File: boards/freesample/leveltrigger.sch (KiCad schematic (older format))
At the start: 23 parts, among them U10 PI6C59S6005, U9 HMC675LP3E

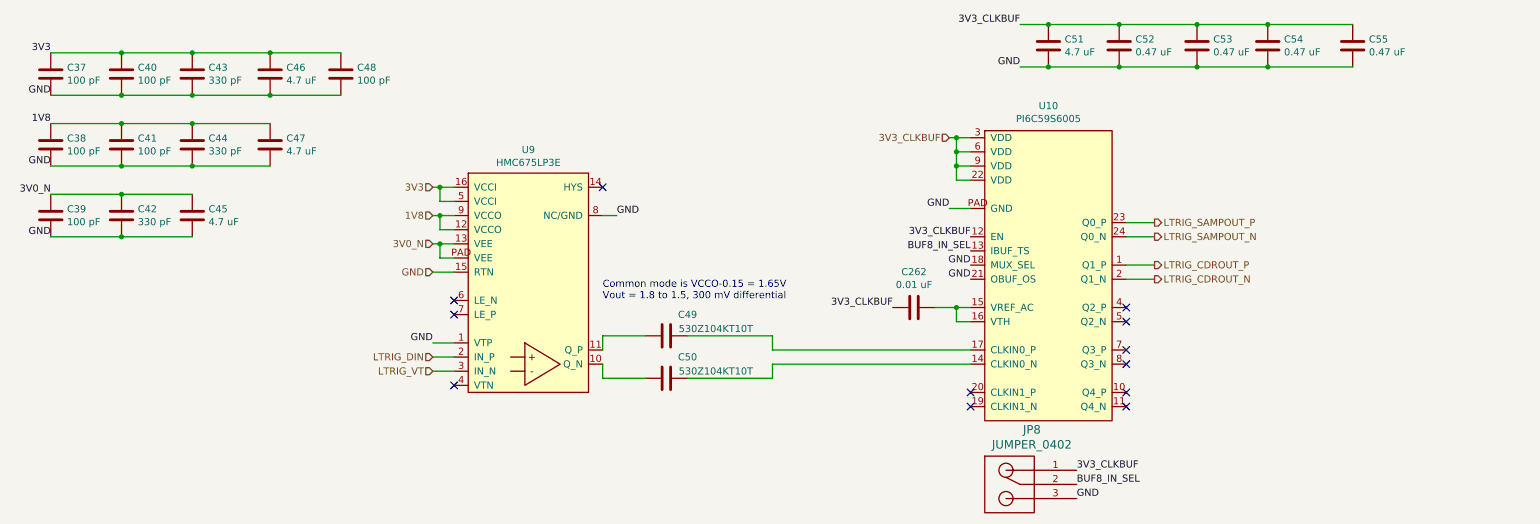
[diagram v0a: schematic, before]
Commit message: Added more test points. Started picking packages for passives. Continued schematic review.
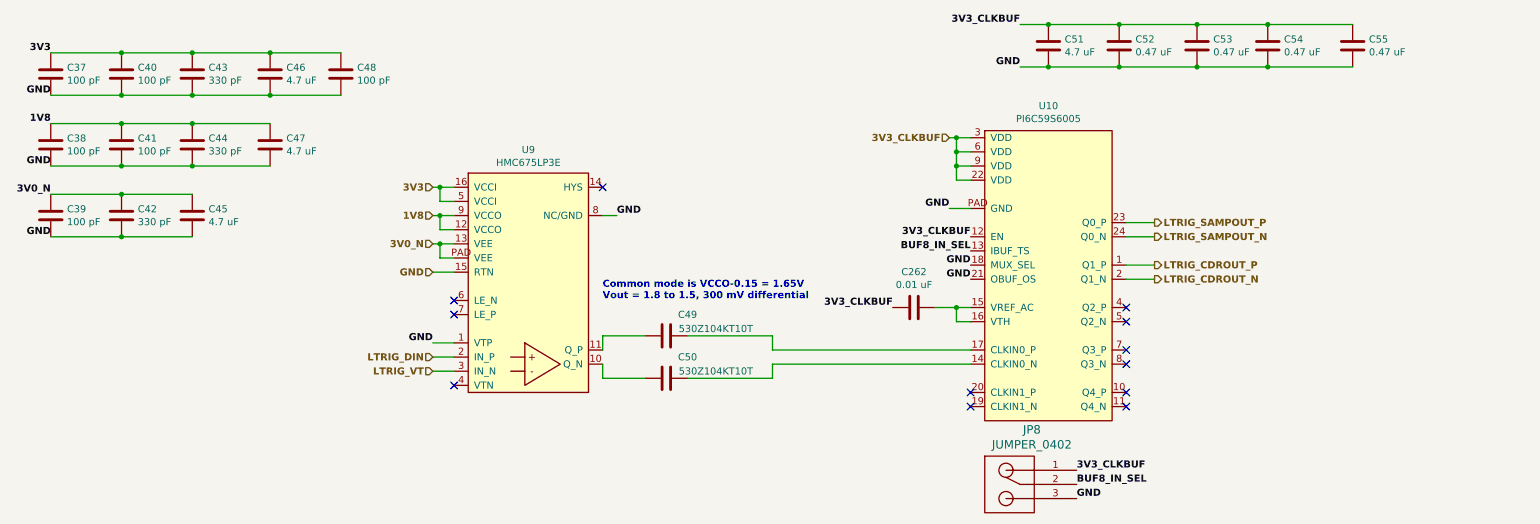
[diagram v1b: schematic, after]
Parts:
- C262, C52, C53, C54, C55: footprint (none) -> azonenberg_pcb:EIA_0402_CAP_NOSILK
- C37, C38, C39, C40, C41, C42, C43, C44, C48, C49, C50: footprint (none) -> azonenberg_pcb:EIA_0201_CAP_NOSILK
- C45, C46, C47, C51: footprint (none) -> azonenberg_pcb:EIA_0603_CAP_NOSILK
- JP8: footprint (none) -> azonenberg_pcb:EIA_0402_JUMPER
- U10: footprint (none) -> azonenberg_pcb:QFN_24_0.5MM_4x4MM
- U9: footprint (none) -> azonenberg_pcb:QFN_16_0.5MM_3x3MM
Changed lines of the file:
@@
 Comment4 ""
 $EndDescr
-Text HLabel 3750 3000 0    50   Input ~ 0
+Text HLabel 3750 3000 0    50   Input ~ 6
 LTRIG_DIN
-Text HLabel 8850 2350 2    50   Output ~ 0
+Text HLabel 8850 2350 2    50   Output ~ 6
 LTRIG_CDROUT_P
-Text HLabel 8850 2450 2    50   Output ~ 0
+Text HLabel 8850 2450 2    50   Output ~ 6
 LTRIG_CDROUT_N
-Text HLabel 3750 1800 0    50   Input ~ 0
+Text HLabel 3750 1800 0    50   Input ~ 6
 3V3
-Text HLabel 3750 2200 0    50   Input ~ 0
+Text HLabel 3750 2200 0    50   Input ~ 6
 3V0_N
-Text HLabel 3750 2400 0    50   Input ~ 0
-GND
-Text HLabel 3750 2000 0    50   Input ~ 0
+Text HLabel 3750 2400 0    50   Input ~ 6
+GND
+Text HLabel 3750 2000 0    50   Input ~ 6
 1V8
-Text HLabel 3750 3100 0    50   Input ~ 0
+Text HLabel 3750 3100 0    50   Input ~ 6
 LTRIG_VT
-Text HLabel 8850 2050 2    50   Output ~ 0
+Text HLabel 8850 2050 2    50   Output ~ 6
 LTRIG_SAMPOUT_P
-Text HLabel 8850 2150 2    50   Output ~ 0
+Text HLabel 8850 2150 2    50   Output ~ 6
 LTRIG_SAMPOUT_N
 $Comp
@@
 F 0 "U9" H 4425 4965 50  0000 C CNN
 F 1 "HMC675LP3E" H 4425 4874 50  0000 C CNN
-F 2 "" H 4000 3250 50  0001 C CNN
+F 2 "azonenberg_pcb:QFN_16_0.5MM_3x3MM" H 4000 3250 50  0001 C CNN
 F 3 "" H 4000 3250 50  0001 C CNN
 	1    4000 3250
@@
 F 0 "C43" H 2165 1046 50  0000 L CNN
 F 1 "330 pF" H 2165 955 50  0000 L CNN
-F 2 "" H 2088 850 50  0001 C CNN
+F 2 "azonenberg_pcb:EIA_0201_CAP_NOSILK" H 2088 850 50  0001 C CNN
 F 3 "" H 2050 1000 50  0001 C CNN
 	1    2050 1000
@@
 F 0 "C40" H 1665 1046 50  0000 L CNN
 F 1 "100 pF" H 1665 955 50  0000 L CNN
-F 2 "" H 1588 850 50  0001 C CNN
+F 2 "azonenberg_pcb:EIA_0201_CAP_NOSILK" H 1588 850 50  0001 C CNN
 F 3 "" H 1550 1000 50  0001 C CNN
 	1    1550 1000
@@
 F 0 "C37" H 1165 1046 50  0000 L CNN
 F 1 "100 pF" H 1165 955 50  0000 L CNN
-F 2 "" H 1088 850 50  0001 C CNN
+F 2 "azonenberg_pcb:EIA_0201_CAP_NOSILK" H 1088 850 50  0001 C CNN
 F 3 "" H 1050 1000 50  0001 C CNN
 	1    1050 1000
 	1    0    0    -1
 $EndComp
-Text Label 1050 1150 2    50   ~ 0
-GND
-Text Label 1050 850  2    50   ~ 0
+Text Label 1050 1150 2    50   ~ 6
+GND
+Text Label 1050 850  2    50   ~ 6
 3V3
 $Comp
@@
 F 0 "C46" H 2715 1046 50  0000 L CNN
 F 1 "4.7 uF" H 2715 955 50  0000 L CNN
-F 2 "" H 2638 850 50  0001 C CNN
+F 2 "azonenberg_pcb:EIA_0603_CAP_NOSILK" H 2638 850 50  0001 C CNN
 F 3 "" H 2600 1000 50  0001 C CNN
 	1    2600 1000
@@
 F 0 "C48" H 3215 1046 50  0000 L CNN
 F 1 "100 pF" H 3215 955 50  0000 L CNN
-F 2 "" H 3138 850 50  0001 C CNN
+F 2 "azonenberg_pcb:EIA_0201_CAP_NOSILK" H 3138 850 50  0001 C CNN
 F 3 "" H 3100 1000 50  0001 C CNN
 	1    3100 1000
@@
 F 0 "C44" H 2165 1546 50  0000 L CNN
 F 1 "330 pF" H 2165 1455 50  0000 L CNN
-F 2 "" H 2088 1350 50  0001 C CNN
+F 2 "azonenberg_pcb:EIA_0201_CAP_NOSILK" H 2088 1350 50  0001 C CNN
 F 3 "" H 2050 1500 50  0001 C CNN
 	1    2050 1500
@@
 F 0 "C41" H 1665 1546 50  0000 L CNN
 F 1 "100 pF" H 1665 1455 50  0000 L CNN
-F 2 "" H 1588 1350 50  0001 C CNN
+F 2 "azonenberg_pcb:EIA_0201_CAP_NOSILK" H 1588 1350 50  0001 C CNN
 F 3 "" H 1550 1500 50  0001 C CNN
 	1    1550 1500
@@
 F 0 "C38" H 1165 1546 50  0000 L CNN
 F 1 "100 pF" H 1165 1455 50  0000 L CNN
-F 2 "" H 1088 1350 50  0001 C CNN
+F 2 "azonenberg_pcb:EIA_0201_CAP_NOSILK" H 1088 1350 50  0001 C CNN
 F 3 "" H 1050 1500 50  0001 C CNN
 	1    1050 1500
 	1    0    0    -1
 $EndComp
-Text Label 1050 1650 2    50   ~ 0
-GND
-Text Label 1050 1350 2    50   ~ 0
+Text Label 1050 1650 2    50   ~ 6
+GND
+Text Label 1050 1350 2    50   ~ 6
 1V8
 $Comp
@@
 F 0 "C47" H 2715 1546 50  0000 L CNN
 F 1 "4.7 uF" H 2715 1455 50  0000 L CNN
-F 2 "" H 2638 1350 50  0001 C CNN
+F 2 "azonenberg_pcb:EIA_0603_CAP_NOSILK" H 2638 1350 50  0001 C CNN
 F 3 "" H 2600 1500 50  0001 C CNN
 	1    2600 1500
@@
 Wire Wire Line
 	2050 1650 2600 1650
-Text Label 1050 1850 2    50   ~ 0
+Text Label 1050 1850 2    50   ~ 6
 3V0_N
 $Comp
@@
 F 0 "C39" H 1165 2046 50  0000 L CNN
 F 1 "100 pF" H 1165 1955 50  0000 L CNN
-F 2 "" H 1088 1850 50  0001 C CNN
+F 2 "azonenberg_pcb:EIA_0201_CAP_NOSILK" H 1088 1850 50  0001 C CNN
 F 3 "" H 1050 2000 50  0001 C CNN
 	1    1050 2000
@@
 F 0 "C42" H 1665 2046 50  0000 L CNN
 F 1 "330 pF" H 1665 1955 50  0000 L CNN
-F 2 "" H 1588 1850 50  0001 C CNN
+F 2 "azonenberg_pcb:EIA_0201_CAP_NOSILK" H 1588 1850 50  0001 C CNN
 F 3 "" H 1550 2000 50  0001 C CNN
 	1    1550 2000
@@
 F 0 "C45" H 2165 2046 50  0000 L CNN
 F 1 "4.7 uF" H 2165 1955 50  0000 L CNN
-F 2 "" H 2088 1850 50  0001 C CNN
+F 2 "azonenberg_pcb:EIA_0603_CAP_NOSILK" H 2088 1850 50  0001 C CNN
 F 3 "" H 2050 2000 50  0001 C CNN
 	1    2050 2000
@@
 Wire Wire Line
 	1550 2150 1050 2150
-Text Label 1050 2150 2    50   ~ 0
+Text Label 1050 2150 2    50   ~ 6
 GND
 Wire Wire Line
@@
 	3800 2000 3900 2000
 NoConn ~ 4950 1800
-Text Label 5050 2000 0    50   ~ 0
+Text Label 5050 2000 0    50   ~ 6
 GND
 Wire Wire Line
@@
 F 0 "U10" H 8100 5675 50  0000 C CNN
 F 1 "PI6C59S6005" H 8100 5584 50  0000 C CNN
-F 2 "" H 7650 3150 50  0001 C CNN
+F 2 "azonenberg_pcb:QFN_24_0.5MM_4x4MM" H 7650 3150 50  0001 C CNN
 F 3 "" H 7650 3150 50  0001 C CNN
 	1    7650 3450
@@
 F 0 "C51" H 8215 846 50  0000 L CNN
 F 1 "4.7 uF" H 8215 755 50  0000 L CNN
-F 2 "" H 8138 650 50  0001 C CNN
+F 2 "azonenberg_pcb:EIA_0603_CAP_NOSILK" H 8138 650 50  0001 C CNN
 F 3 "" H 8100 800 50  0001 C CNN
 	1    8100 800
@@
 F 0 "C52" H 8715 846 50  0000 L CNN
 F 1 "0.47 uF" H 8715 755 50  0000 L CNN
-F 2 "" H 8638 650 50  0001 C CNN
+F 2 "azonenberg_pcb:EIA_0402_CAP_NOSILK" H 8638 650 50  0001 C CNN
 F 3 "" H 8600 800 50  0001 C CNN
 	1    8600 800
@@
 F 0 "C54" H 9765 846 50  0000 L CNN
 F 1 "0.47 uF" H 9765 755 50  0000 L CNN
-F 2 "" H 9688 650 50  0001 C CNN
+F 2 "azonenberg_pcb:EIA_0402_CAP_NOSILK" H 9688 650 50  0001 C CNN
 F 3 "" H 9650 800 50  0001 C CNN
 	1    9650 800
@@
 Wire Wire Line
 	8600 950  8100 950
-Text Label 7900 650  2    50   ~ 0
+Text Label 7900 650  2    50   ~ 6
 3V3_CLKBUF
 Wire Wire Line
 	7900 650  8100 650
 Connection ~ 8100 650
-Text Label 7900 950  2    50   ~ 0
+Text Label 7900 950  2    50   ~ 6
 GND
 Wire Wire Line
@@
 F 0 "C53" H 9265 846 50  0000 L CNN
 F 1 "0.47 uF" H 9265 755 50  0000 L CNN
-F 2 "" H 9188 650 50  0001 C CNN
+F 2 "azonenberg_pcb:EIA_0402_CAP_NOSILK" H 9188 650 50  0001 C CNN
 F 3 "" H 9150 800 50  0001 C CNN
 	1    9150 800
@@
 F 0 "C55" H 10365 846 50  0000 L CNN
 F 1 "0.47 uF" H 10365 755 50  0000 L CNN
-F 2 "" H 10288 650 50  0001 C CNN
+F 2 "azonenberg_pcb:EIA_0402_CAP_NOSILK" H 10288 650 50  0001 C CNN
 F 3 "" H 10250 800 50  0001 C CNN
 	1    10250 800
@@
 Wire Wire Line
 	3900 3000 3750 3000
-Text Label 3750 2900 2    50   ~ 0
+Text Label 3750 2900 2    50   ~ 6
 GND
 Wire Wire Line
@@
 F 0 "C49" V 5250 3000 50  0000 C CNN
 F 1 "530Z104KT10T" V 5350 3200 50  0000 C CNN
-F 2 "" H 5438 2700 50  0001 C CNN
+F 2 "azonenberg_pcb:EIA_0201_CAP_NOSILK" H 5438 2700 50  0001 C CNN
 F 3 "" H 5400 2850 50  0001 C CNN
 	1    5400 2850
@@
 F 0 "C50" V 5250 3300 50  0000 C CNN
 F 1 "530Z104KT10T" V 5350 3500 50  0000 C CNN
-F 2 "" H 5438 3000 50  0001 C CNN
+F 2 "azonenberg_pcb:EIA_0201_CAP_NOSILK" H 5438 3000 50  0001 C CNN
 F 3 "" H 5400 3150 50  0001 C CNN
 	1    5400 3150
@@
 	7450 1750 7550 1750
 Connection ~ 7450 1650
-Text Label 7400 1950 2    50   ~ 0
+Text Label 7400 1950 2    50   ~ 6
 GND
 Wire Wire Line
@@
 Wire Wire Line
 	8650 2450 8850 2450
-Text Notes 4950 2600 0    50   ~ 0
+Text Notes 4950 2600 0    50   ~ 6
 Common mode is VCCO-0.15 = 1.65V\nVout = 1.8 to 1.5, 300 mV differential
-Text HLabel 7400 1450 0    50   Input ~ 0
+Text HLabel 7400 1450 0    50   Input ~ 6
 3V3_CLKBUF
-Text Label 7550 2150 2    50   ~ 0
+Text Label 7550 2150 2    50   ~ 6
 3V3_CLKBUF
 NoConn ~ 7550 3250
 NoConn ~ 7550 3350
-Text Label 7550 2350 2    50   ~ 0
-GND
-Text Label 7550 2450 2    50   ~ 0
+Text Label 7550 2350 2    50   ~ 6
+GND
+Text Label 7550 2450 2    50   ~ 6
 GND
 Wire Wire Line
@@
 F 0 "C262" V 6898 2650 50  0000 C CNN
 F 1 "0.01 uF" V 6989 2650 50  0000 C CNN
-F 2 "" H 7188 2500 50  0001 C CNN
+F 2 "azonenberg_pcb:EIA_0402_CAP_NOSILK" H 7188 2500 50  0001 C CNN
 F 3 "" H 7150 2650 50  0001 C CNN
 	1    7150 2650
@@
 	7300 2650 7450 2650
 Connection ~ 7450 2650
-Text Label 7000 2650 2    50   ~ 0
+Text Label 7000 2650 2    50   ~ 6
 3V3_CLKBUF
 $Comp
@@
 F 0 "JP8" H 7983 4687 60  0000 C CNN
 F 1 "JUMPER_0402" H 7983 4581 60  0000 C CNN
-F 2 "" H 8000 4100 60  0000 C CNN
+F 2 "azonenberg_pcb:EIA_0402_JUMPER" H 8000 4100 60  0001 C CNN
 F 3 "" H 8000 4100 60  0000 C CNN
 	1    8000 4100
 	1    0    0    -1
 $EndComp
-Text Label 8300 3900 0    50   ~ 0
+Text Label 8300 3900 0    50   ~ 6
 BUF8_IN_SEL
-Text Label 8300 3800 0    50   ~ 0
+Text Label 8300 3800 0    50   ~ 6
 3V3_CLKBUF
-Text Label 8300 4000 0    50   ~ 0
-GND
-Text Label 7550 2250 2    50   ~ 0
+Text Label 8300 4000 0    50   ~ 6
+GND
+Text Label 7550 2250 2    50   ~ 6
 BUF8_IN_SEL
 $EndSCHEMATC

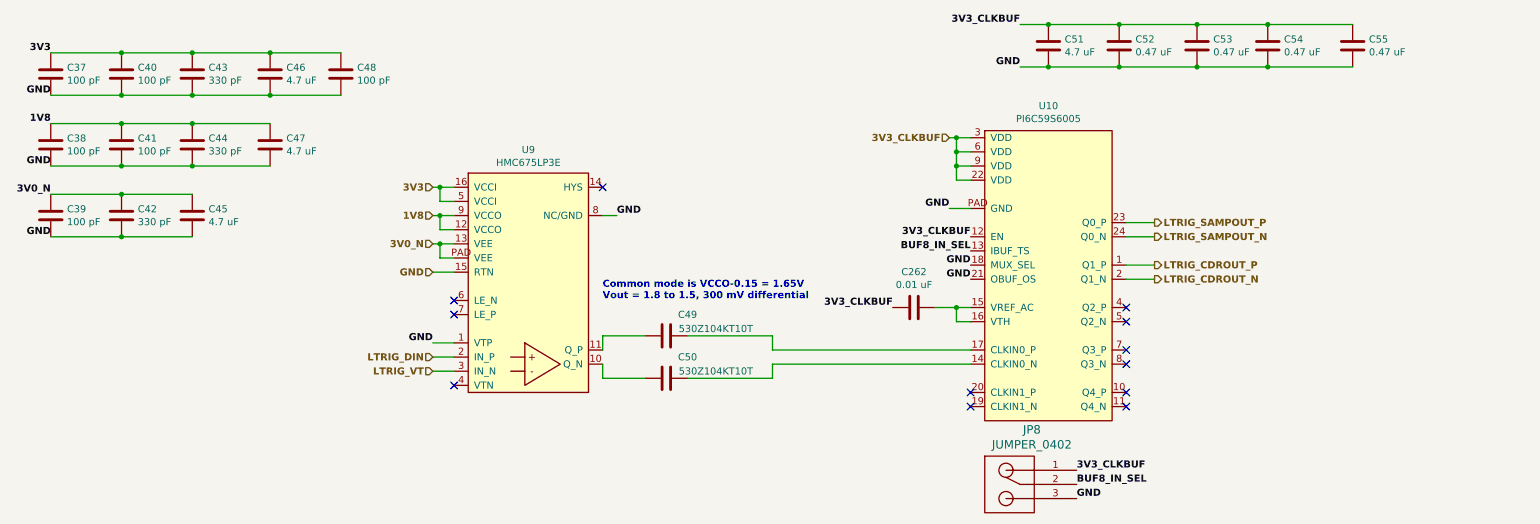
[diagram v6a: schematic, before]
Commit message: Tweaks to PLL and CDR layout, swapped a few signals around. Began work on level trigger and ADC layout.
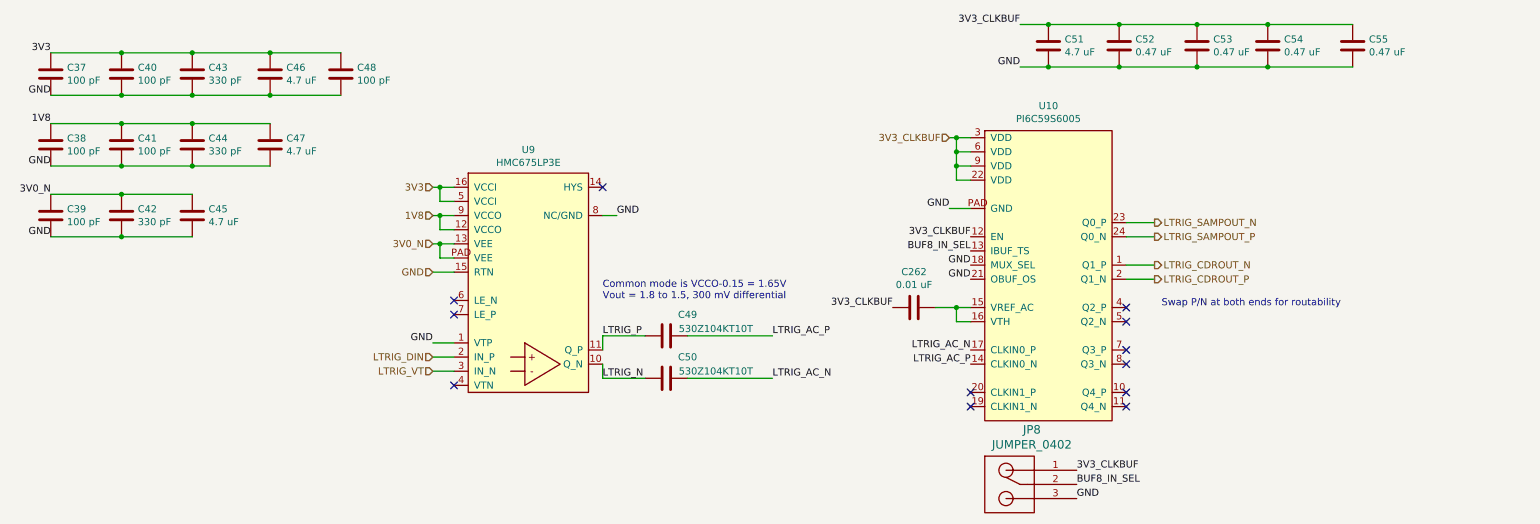
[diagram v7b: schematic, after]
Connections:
- net LTRIG_CDROUT_N: now also U10.1 (Q1_P); no longer U10.2 (Q1_N)
- net LTRIG_CDROUT_P: now also U10.2 (Q1_N); no longer U10.1 (Q1_P)
- net LTRIG_SAMPOUT_N: now also U10.23 (Q0_P); no longer U10.24 (Q0_N)
- net LTRIG_SAMPOUT_P: now also U10.24 (Q0_N); no longer U10.23 (Q0_P)
- net LTRIG_N: now reaches C50.2, U9.10 (Q_N)
- net LTRIG_P: now reaches C49.2, U9.11 (Q_P)
- net LTRIG_AC_N: now reaches C50.1
- net LTRIG_AC_N: now also U10.17 (CLKIN0_P); no longer U10.14 (CLKIN0_N)
- net LTRIG_AC_P: now reaches C49.1
- net LTRIG_AC_P: now also U10.14 (CLKIN0_N); no longer U10.17 (CLKIN0_P)
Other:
- note added: "Swap P/N at both ends for routability"
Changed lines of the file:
@@
 Comment4 ""
 $EndDescr
-Text HLabel 3750 3000 0    50   Input ~ 10
+Text HLabel 3750 3000 0    50   Input ~ 0
 LTRIG_DIN
-Text HLabel 8850 2350 2    50   Output ~ 10
+Text HLabel 8850 2450 2    50   Output ~ 0
 LTRIG_CDROUT_P
-Text HLabel 8850 2450 2    50   Output ~ 10
+Text HLabel 8850 2350 2    50   Output ~ 0
 LTRIG_CDROUT_N
-Text HLabel 3750 1800 0    50   Input ~ 10
+Text HLabel 3750 1800 0    50   Input ~ 0
 3V3
-Text HLabel 3750 2200 0    50   Input ~ 10
+Text HLabel 3750 2200 0    50   Input ~ 0
 3V0_N
-Text HLabel 3750 2400 0    50   Input ~ 10
-GND
-Text HLabel 3750 2000 0    50   Input ~ 10
+Text HLabel 3750 2400 0    50   Input ~ 0
+GND
+Text HLabel 3750 2000 0    50   Input ~ 0
 1V8
-Text HLabel 3750 3100 0    50   Input ~ 10
+Text HLabel 3750 3100 0    50   Input ~ 0
 LTRIG_VT
-Text HLabel 8850 2050 2    50   Output ~ 10
+Text HLabel 8850 2150 2    50   Output ~ 0
 LTRIG_SAMPOUT_P
-Text HLabel 8850 2150 2    50   Output ~ 10
+Text HLabel 8850 2050 2    50   Output ~ 0
 LTRIG_SAMPOUT_N
 $Comp
@@
 	1    0    0    -1
 $EndComp
-Text Label 1050 1150 2    50   ~ 10
-GND
-Text Label 1050 850  2    50   ~ 10
+Text Label 1050 1150 2    50   ~ 0
+GND
+Text Label 1050 850  2    50   ~ 0
 3V3
 $Comp
@@
 	1    0    0    -1
 $EndComp
-Text Label 1050 1650 2    50   ~ 10
-GND
-Text Label 1050 1350 2    50   ~ 10
+Text Label 1050 1650 2    50   ~ 0
+GND
+Text Label 1050 1350 2    50   ~ 0
 1V8
 $Comp
@@
 Wire Wire Line
 	2050 1650 2600 1650
-Text Label 1050 1850 2    50   ~ 10
+Text Label 1050 1850 2    50   ~ 0
 3V0_N
 $Comp
@@
 Wire Wire Line
 	1550 2150 1050 2150
-Text Label 1050 2150 2    50   ~ 10
+Text Label 1050 2150 2    50   ~ 0
 GND
 Wire Wire Line
@@
 	3800 2000 3900 2000
 NoConn ~ 4950 1800
-Text Label 5050 2000 0    50   ~ 10
+Text Label 5050 2000 0    50   ~ 0
 GND
 Wire Wire Line
@@
 Wire Wire Line
 	8600 950  8100 950
-Text Label 7900 650  2    50   ~ 10
+Text Label 7900 650  2    50   ~ 0
 3V3_CLKBUF
 Wire Wire Line
 	7900 650  8100 650
 Connection ~ 8100 650
-Text Label 7900 950  2    50   ~ 10
+Text Label 7900 950  2    50   ~ 0
 GND
 Wire Wire Line
@@
 Wire Wire Line
 	3900 3000 3750 3000
-Text Label 3750 2900 2    50   ~ 10
+Text Label 3750 2900 2    50   ~ 0
 GND
 Wire Wire Line
@@
 	5550 3150 6150 3150
 Wire Wire Line
-	6150 3150 6150 3050
-Wire Wire Line
-	6150 3050 7550 3050
-Wire Wire Line
 	5550 2850 6150 2850
-Wire Wire Line
-	6150 2850 6150 2950
-Wire Wire Line
-	6150 2950 7550 2950
 Wire Wire Line
 	7400 1450 7450 1450
@@
 	7450 1750 7550 1750
 Connection ~ 7450 1650
-Text Label 7400 1950 2    50   ~ 10
+Text Label 7400 1950 2    50   ~ 0
 GND
 Wire Wire Line
@@
 Wire Wire Line
 	8650 2450 8850 2450
-Text Notes 4950 2600 0    50   ~ 10
+Text Notes 4950 2600 0    50   ~ 0
 Common mode is VCCO-0.15 = 1.65V\nVout = 1.8 to 1.5, 300 mV differential
-Text HLabel 7400 1450 0    50   Input ~ 10
+Text HLabel 7400 1450 0    50   Input ~ 0
 3V3_CLKBUF
-Text Label 7550 2150 2    50   ~ 10
+Text Label 7550 2150 2    50   ~ 0
 3V3_CLKBUF
 NoConn ~ 7550 3250
 NoConn ~ 7550 3350
-Text Label 7550 2350 2    50   ~ 10
-GND
-Text Label 7550 2450 2    50   ~ 10
+Text Label 7550 2350 2    50   ~ 0
+GND
+Text Label 7550 2450 2    50   ~ 0
 GND
 Wire Wire Line
@@
 	7300 2650 7450 2650
 Connection ~ 7450 2650
-Text Label 7000 2650 2    50   ~ 10
+Text Label 7000 2650 2    50   ~ 0
 3V3_CLKBUF
 $Comp
@@
 	1    0    0    -1
 $EndComp
-Text Label 8300 3900 0    50   ~ 10
+Text Label 8300 3900 0    50   ~ 0
 BUF8_IN_SEL
-Text Label 8300 3800 0    50   ~ 10
+Text Label 8300 3800 0    50   ~ 0
 3V3_CLKBUF
-Text Label 8300 4000 0    50   ~ 10
-GND
-Text Label 7550 2250 2    50   ~ 10
+Text Label 8300 4000 0    50   ~ 0
+GND
+Text Label 7550 2250 2    50   ~ 0
 BUF8_IN_SEL
+Text Label 4950 2850 0    50   ~ 0
+LTRIG_P
+Text Label 4950 3150 0    50   ~ 0
+LTRIG_N
+Text Label 6150 2850 0    50   ~ 0
+LTRIG_AC_P
+Text Label 6150 3150 0    50   ~ 0
+LTRIG_AC_N
+Text Label 7550 2950 2    50   ~ 0
+LTRIG_AC_N
+Text Label 7550 3050 2    50   ~ 0
+LTRIG_AC_P
+Text Notes 8900 2650 0    50   ~ 0
+Swap P/N at both ends for routability
 $EndSCHEMATC
